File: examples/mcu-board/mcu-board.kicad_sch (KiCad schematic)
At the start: 11 parts, among them J1 5V_IN, J2 PROG/IO, SW1 Reset, U1 MCU, U2 AMS1117-3.3

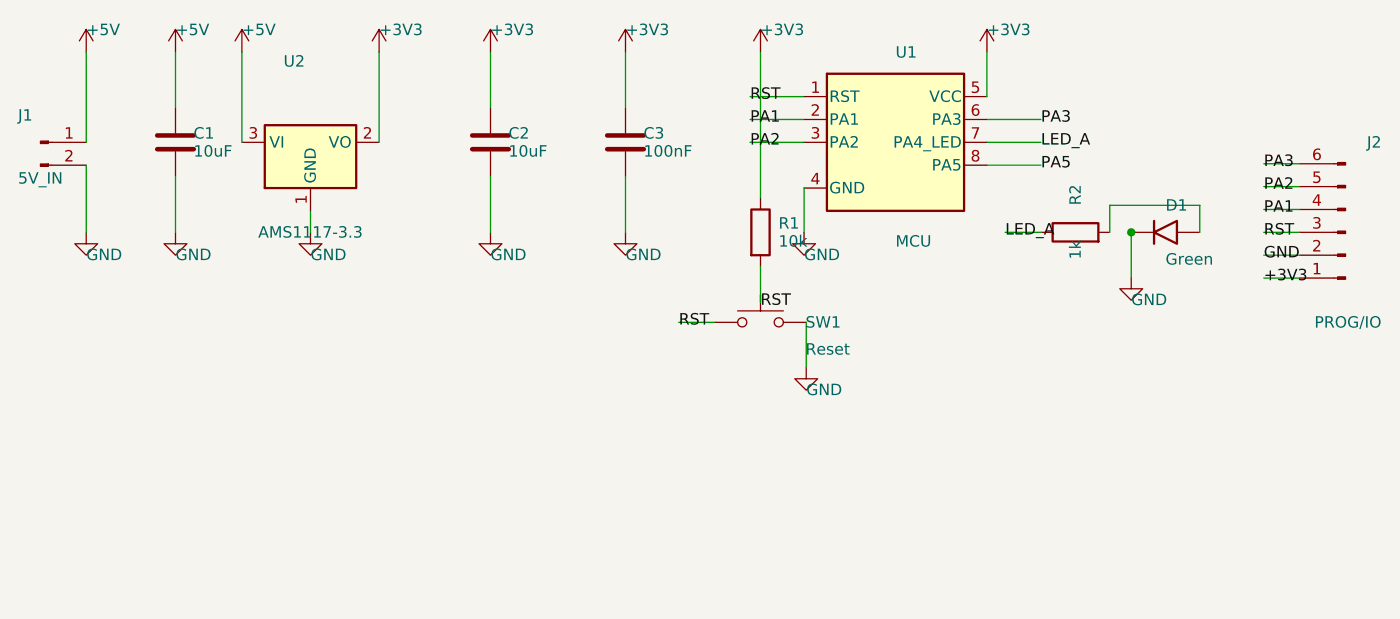
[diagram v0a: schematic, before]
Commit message: demo: mcu-board temp sensor + routing rework
Demo diff for the kicadiff PR-triggered workflow. Adds a temperature
sensor IC near the MCU, reworks tracking around the LDO, and wiggles
silkscreen labels — gives the visual diff something to chew on with
all three categories (add / delete / change) present.

Not a real design change. Branch exists to exercise the kicad-pr-diff
workflow against a real PR context.

Co-Authored-By: Claude Opus 4.7 (1M context) <noreply@anthropic.com>
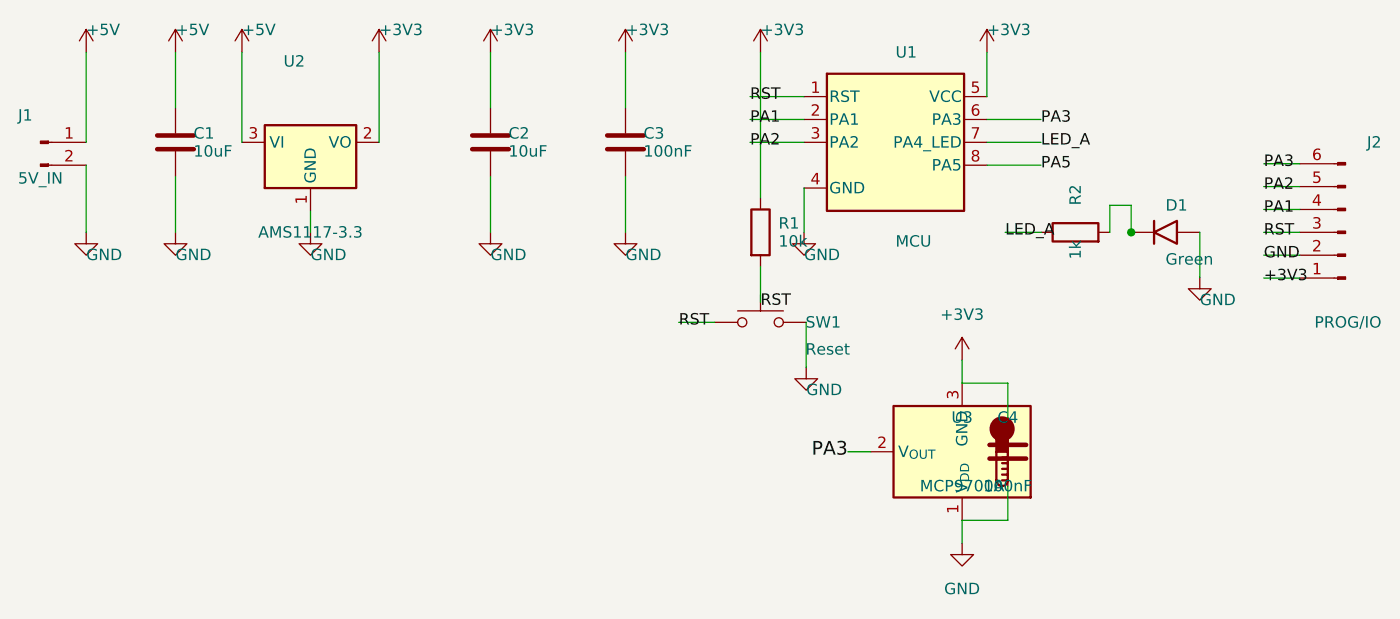
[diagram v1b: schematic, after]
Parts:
- added C4: 100nF, Capacitor_SMD:C_0805_2012Metric, symbol Device:C
- added U3: MCP9700A, Package_TO_SOT_SMD:SOT-23, symbol Sensor_Temperature:MCP9700Ax-ETT
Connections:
- net +3V3: now also C4.1
- net GND: now also D1.2 (A), C4.2; no longer D1.1 (K)
- net at R2.2: now also D1.1 (K); no longer D1.2 (A)
